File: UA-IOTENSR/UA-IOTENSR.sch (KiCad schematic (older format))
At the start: 2 parts, among them SW101 SW_MEC_5G, U101 ESP32-S2-WROOM

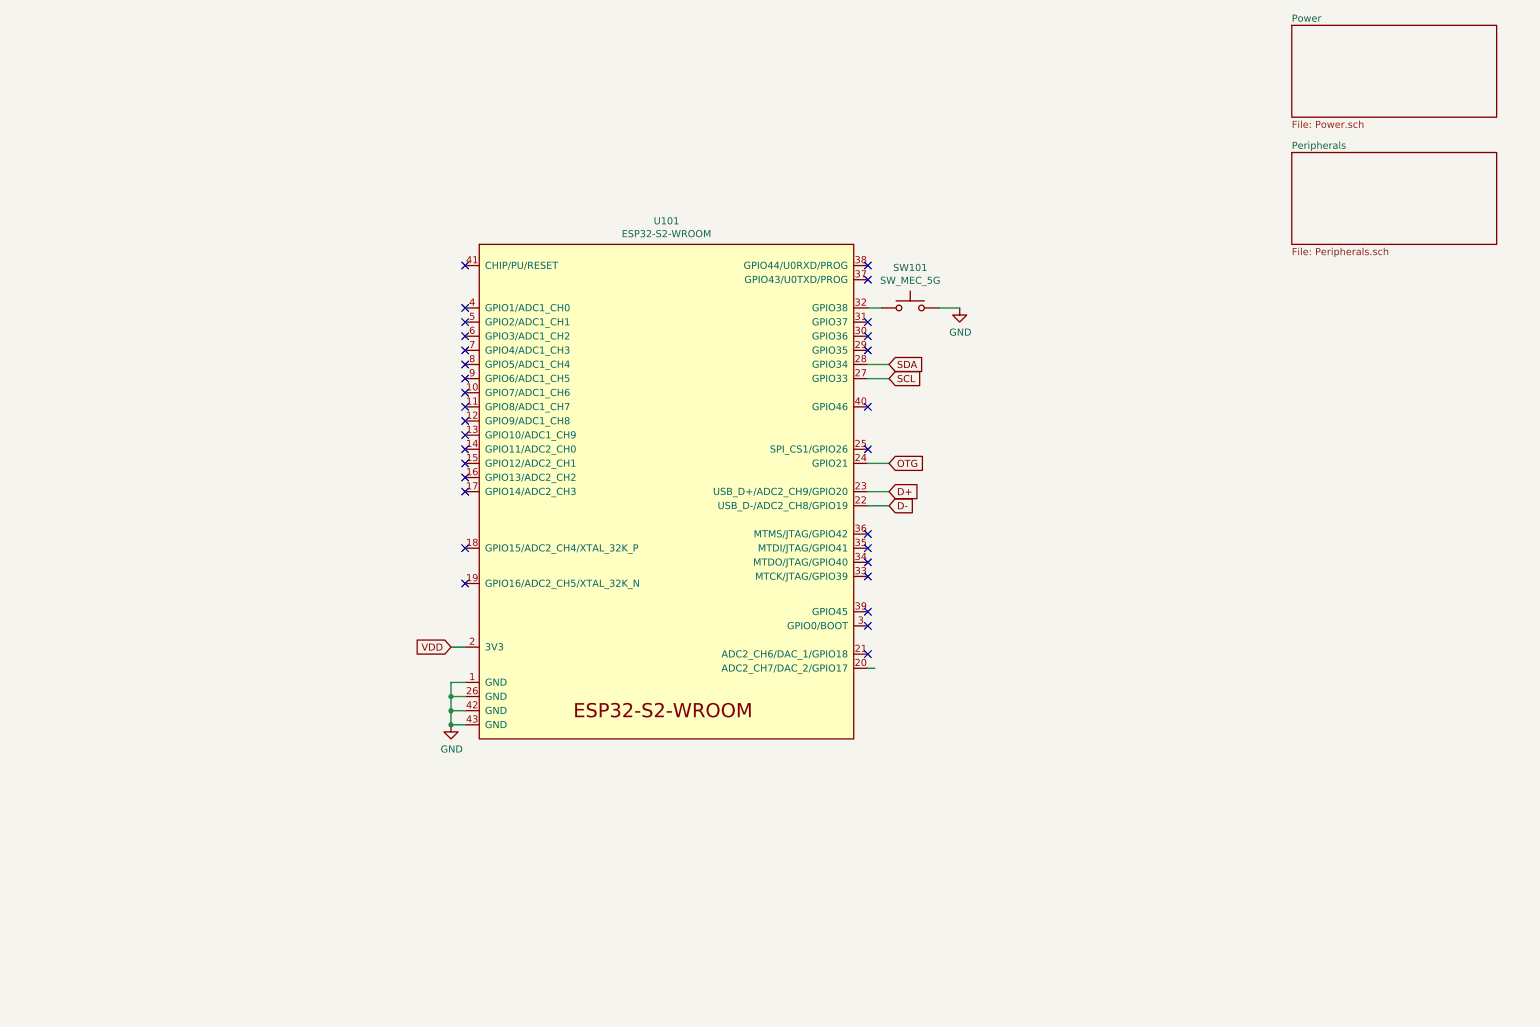
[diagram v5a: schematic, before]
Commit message: updated symbols; changed vdd to 3v3 global for pcb design later
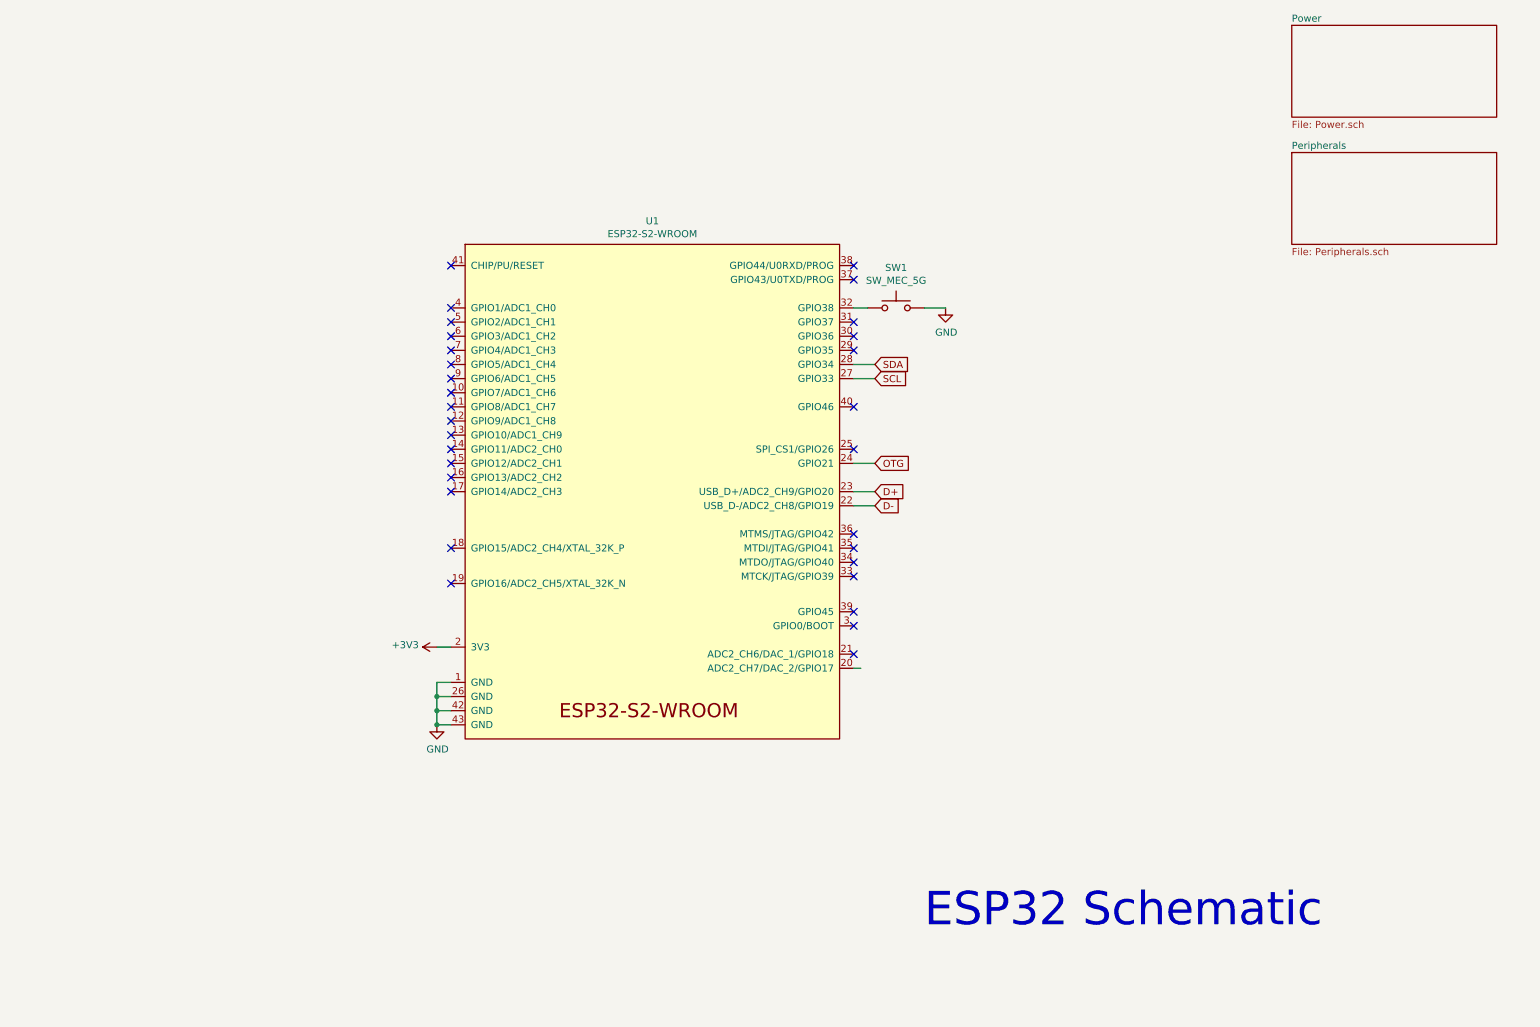
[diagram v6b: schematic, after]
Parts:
- renumbered SW101 to SW1, U101 to U1
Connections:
- net labels added: +3V3
- net labels removed: VDD
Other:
- note added: "ESP32 Schematic"
- moved on the sheet: SW1, U1
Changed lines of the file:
@@
 $EndDescr
 $Comp
-L power:GND #PWR0101
+L power:GND #PWR01
 U 1 1 61961638
-P 3650 5550
-F 0 "#PWR0101" H 3650 5300 50  0001 C CNN
-F 1 "GND" H 3655 5377 50  0000 C CNN
-F 2 "" H 3650 5550 50  0001 C CNN
-F 3 "" H 3650 5550 50  0001 C CNN
-	1    3650 5550
+P 3550 5550
+F 0 "#PWR01" H 3550 5300 50  0001 C CNN
+F 1 "GND" H 3555 5377 50  0000 C CNN
+F 2 "" H 3550 5550 50  0001 C CNN
+F 3 "" H 3550 5550 50  0001 C CNN
+	1    3550 5550
 	1    0    0    -1
 $EndComp
 Wire Wire Line
-	3650 5350 3750 5350
+	3550 5350 3650 5350
 Wire Wire Line
-	3650 5450 3750 5450
+	3550 5450 3650 5450
 Wire Wire Line
-	3650 5550 3750 5550
+	3550 5550 3650 5550
 $Comp
-L Espressif:ESP32-S2-WROOM U101
+L Espressif:ESP32-S2-WROOM U1
 U 1 1 619E5D94
-P 5150 3900
-F 0 "U101" H 5175 5815 50  0000 C CNN
-F 1 "ESP32-S2-WROOM" H 5175 5724 50  0000 C CNN
-F 2 "Espressif:ESP32-S2-WROOM" H 5150 2000 50  0001 C CNN
-F 3 "https://www.espressif.com/sites/default/files/documentation/esp32-s2-wroom_esp32-s2-wroom-i_datasheet_en.pdf" H 5150 3900 50  0001 C CNN
-	1    5150 3900
+P 5050 3900
+F 0 "U1" H 5075 5815 50  0000 C CNN
+F 1 "ESP32-S2-WROOM" H 5075 5724 50  0000 C CNN
+F 2 "Espressif:ESP32-S2-WROOM" H 5050 2000 50  0001 C CNN
+F 3 "https://www.espressif.com/sites/default/files/documentation/esp32-s2-wroom_esp32-s2-wroom-i_datasheet_en.pdf" H 5050 3900 50  0001 C CNN
+	1    5050 3900
 	1    0    0    -1
 $EndComp
 Wire Wire Line
-	3750 5250 3650 5250
+	3650 5250 3550 5250
 Wire Wire Line
-	3650 5250 3650 5350
-Connection ~ 3650 5350
+	3550 5250 3550 5350
+Connection ~ 3550 5350
 Wire Wire Line
-	3650 5350 3650 5450
-Connection ~ 3650 5450
+	3550 5350 3550 5450
+Connection ~ 3550 5450
 Wire Wire Line
-	3650 5450 3650 5550
-Connection ~ 3650 5550
+	3550 5450 3550 5550
+Connection ~ 3550 5550
 Wire Wire Line
-	6600 3100 6750 3100
-Text GLabel 6750 3100 2    50   Input ~ 0
+	6500 3100 6650 3100
+Text GLabel 6650 3100 2    50   Input ~ 0
 SCL
-Text GLabel 6750 3000 2    50   Input ~ 0
+Text GLabel 6650 3000 2    50   Input ~ 0
 SDA
 Wire Wire Line
-	6600 3000 6750 3000
+	6500 3000 6650 3000
 Wire Wire Line
-	7100 2600 7250 2600
+	7000 2600 7150 2600
 $Comp
-L Switch:SW_MEC_5G SW101
+L Switch:SW_MEC_5G SW1
 U 1 1 619D98CD
-P 6900 2600
-F 0 "SW101" H 6900 2885 50  0000 C CNN
-F 1 "SW_MEC_5G" H 6900 2794 50  0000 C CNN
-F 2 "" H 6900 2800 50  0001 C CNN
-F 3 "http://www.apem.com/int/index.php?controller=attachment&id_attachment=488" H 6900 2800 50  0001 C CNN
-	1    6900 2600
+P 6800 2600
+F 0 "SW1" H 6800 2885 50  0000 C CNN
+F 1 "SW_MEC_5G" H 6800 2794 50  0000 C CNN
+F 2 "" H 6800 2800 50  0001 C CNN
+F 3 "http://www.apem.com/int/index.php?controller=attachment&id_attachment=488" H 6800 2800 50  0001 C CNN
+	1    6800 2600
 	1    0    0    -1
 $EndComp
 Wire Wire Line
-	6600 2600 6700 2600
+	6500 2600 6600 2600
 $Comp
-L power:GND #PWR0102
+L power:GND #PWR02
 U 1 1 61A04BEB
-P 7250 2600
-F 0 "#PWR0102" H 7250 2350 50  0001 C CNN
-F 1 "GND" H 7255 2427 50  0000 C CNN
-F 2 "" H 7250 2600 50  0001 C CNN
-F 3 "" H 7250 2600 50  0001 C CNN
-	1    7250 2600
+P 7150 2600
+F 0 "#PWR02" H 7150 2350 50  0001 C CNN
+F 1 "GND" H 7155 2427 50  0000 C CNN
+F 2 "" H 7150 2600 50  0001 C CNN
+F 3 "" H 7150 2600 50  0001 C CNN
+	1    7150 2600
 	1    0    0    -1
 $EndComp
 Wire Wire Line
-	3750 5000 3650 5000
-Text GLabel 3650 5000 0    50   Input ~ 0
-VDD
-Text GLabel 6750 3900 2    50   Input ~ 0
+	3650 5000 3550 5000
+Text GLabel 6650 3900 2    50   Input ~ 0
 D+
 Wire Wire Line
-	6600 3900 6750 3900
-Text GLabel 6750 4000 2    50   Input ~ 0
+	6500 3900 6650 3900
+Text GLabel 6650 4000 2    50   Input ~ 0
 D-
 Wire Wire Line
-	6600 4000 6750 4000
+	6500 4000 6650 4000
 Wire Wire Line
-	6600 3700 6750 3700
-Text GLabel 6750 3700 2    50   Input ~ 0
+	6500 3700 6650 3700
+Text GLabel 6650 3700 2    50   Input ~ 0
 OTG
 $Sheet
@@
 F1 "Power.sch" 50
 $EndSheet
-NoConn ~ 6600 5050
-NoConn ~ 6600 4850
-NoConn ~ 6600 4750
-NoConn ~ 6600 4500
-NoConn ~ 6600 4400
-NoConn ~ 6600 4300
-NoConn ~ 6600 4200
-NoConn ~ 6600 3600
-NoConn ~ 6600 3300
-NoConn ~ 6600 2900
-NoConn ~ 6600 2800
-NoConn ~ 6600 2700
-NoConn ~ 6600 2400
-NoConn ~ 6600 2300
-NoConn ~ 3750 2300
-NoConn ~ 3750 2600
-NoConn ~ 3750 2700
-NoConn ~ 3750 2800
-NoConn ~ 3750 2900
-NoConn ~ 3750 3000
-NoConn ~ 3750 3100
-NoConn ~ 3750 3200
-NoConn ~ 3750 3300
-NoConn ~ 3750 3400
-NoConn ~ 3750 3500
-NoConn ~ 3750 3600
-NoConn ~ 3750 3700
-NoConn ~ 3750 3800
-NoConn ~ 3750 3900
-NoConn ~ 3750 4300
-NoConn ~ 3750 4550
+NoConn ~ 6500 5050
+NoConn ~ 6500 4850
+NoConn ~ 6500 4750
+NoConn ~ 6500 4500
+NoConn ~ 6500 4400
+NoConn ~ 6500 4300
+NoConn ~ 6500 4200
+NoConn ~ 6500 3600
+NoConn ~ 6500 3300
+NoConn ~ 6500 2900
+NoConn ~ 6500 2800
+NoConn ~ 6500 2700
+NoConn ~ 6500 2400
+NoConn ~ 6500 2300
+NoConn ~ 3650 2300
+NoConn ~ 3650 2600
+NoConn ~ 3650 2700
+NoConn ~ 3650 2800
+NoConn ~ 3650 2900
+NoConn ~ 3650 3000
+NoConn ~ 3650 3100
+NoConn ~ 3650 3200
+NoConn ~ 3650 3300
+NoConn ~ 3650 3400
+NoConn ~ 3650 3500
+NoConn ~ 3650 3600
+NoConn ~ 3650 3700
+NoConn ~ 3650 3800
+NoConn ~ 3650 3900
+NoConn ~ 3650 4300
+NoConn ~ 3650 4550
 Wire Wire Line
-	6600 5150 6650 5150
+	6500 5150 6550 5150
 $Sheet
 S 9600 1500 1450 650
@@
 F1 "Peripherals.sch" 50
 $EndSheet
+Text Notes 7000 7000 0    236  ~ 0
+ESP32 Schematic
+$Comp
+L power:+3V3 #PWR?
+U 1 1 61A18D2A
+P 3550 5000
+F 0 "#PWR?" H 3550 4850 50  0001 C CNN
+F 1 "+3V3" V 3565 5128 50  0000 L CNN
+F 2 "" H 3550 5000 50  0001 C CNN
+F 3 "" H 3550 5000 50  0001 C CNN
+	1    3550 5000
+	0    -1   -1   0
+$EndComp
 $EndSCHEMATC

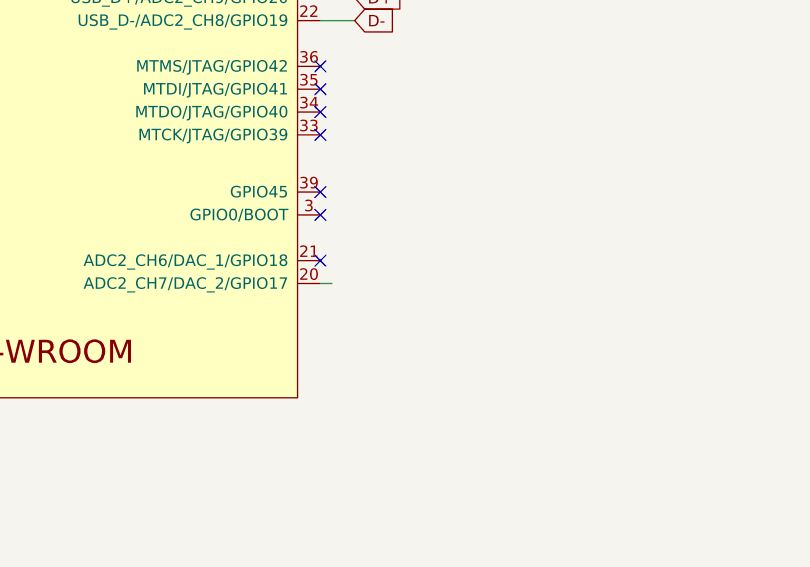
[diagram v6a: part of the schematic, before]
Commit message: Finished LED bar graph array schem
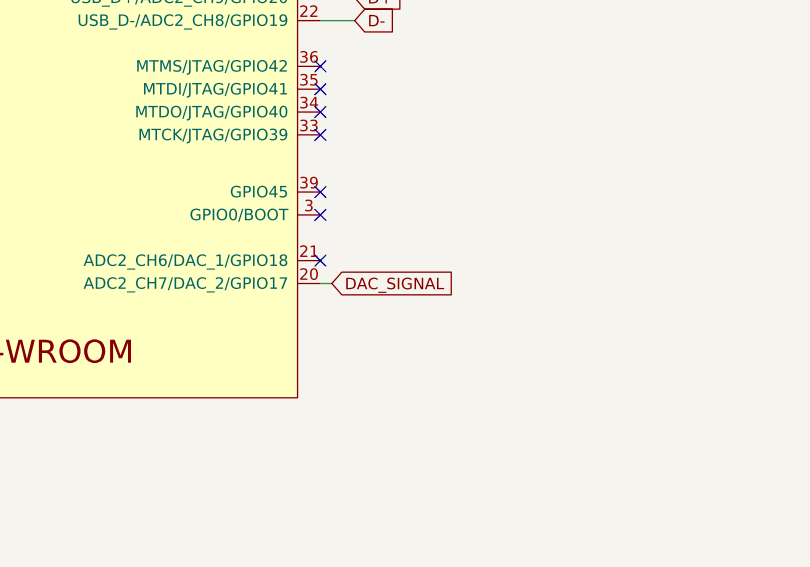
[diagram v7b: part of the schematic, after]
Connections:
- net labels added: DAC_SIGNAL
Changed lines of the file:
@@
 ESP32 Schematic
 $Comp
-L power:+3V3 #PWR?
+L power:+3V3 #PWR06
 U 1 1 61A18D2A
 P 3550 5000
-F 0 "#PWR?" H 3550 4850 50  0001 C CNN
+F 0 "#PWR06" H 3550 4850 50  0001 C CNN
 F 1 "+3V3" V 3565 5128 50  0000 L CNN
 F 2 "" H 3550 5000 50  0001 C CNN
@@
 	0    -1   -1   0
 $EndComp
+Text GLabel 6550 5150 2    50   Input ~ 0
+DAC_SIGNAL
 $EndSCHEMATC
